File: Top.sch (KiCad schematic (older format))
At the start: 0 parts

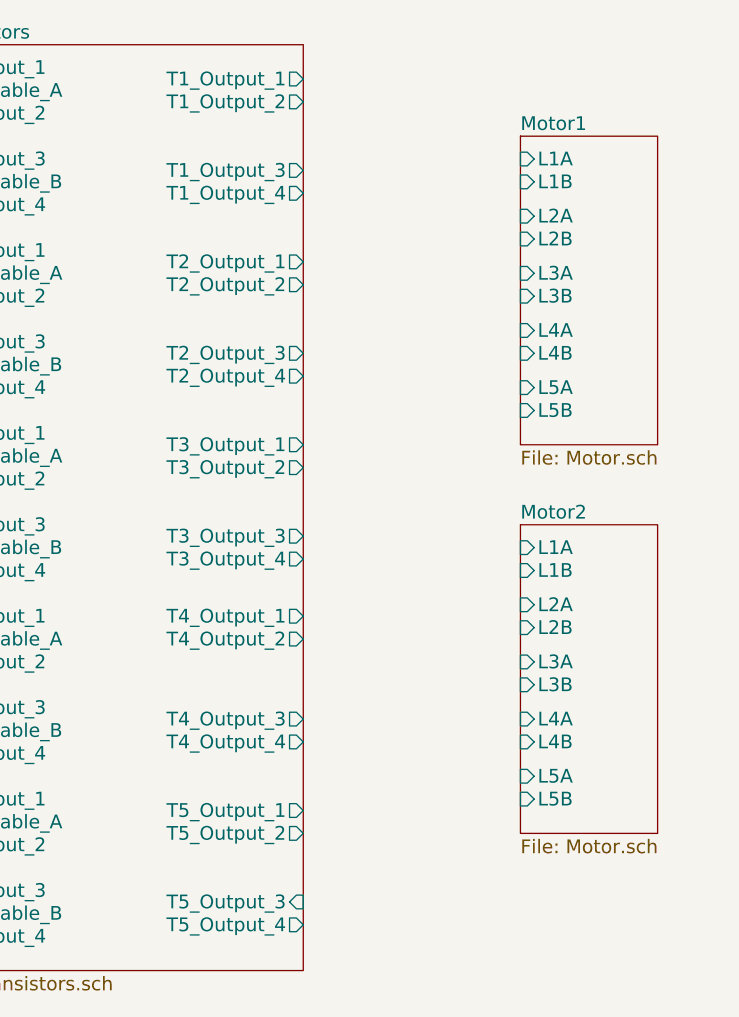
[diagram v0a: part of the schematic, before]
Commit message: Connected hierarchical labels in Top.sch Beautified label order in Transistors.sch
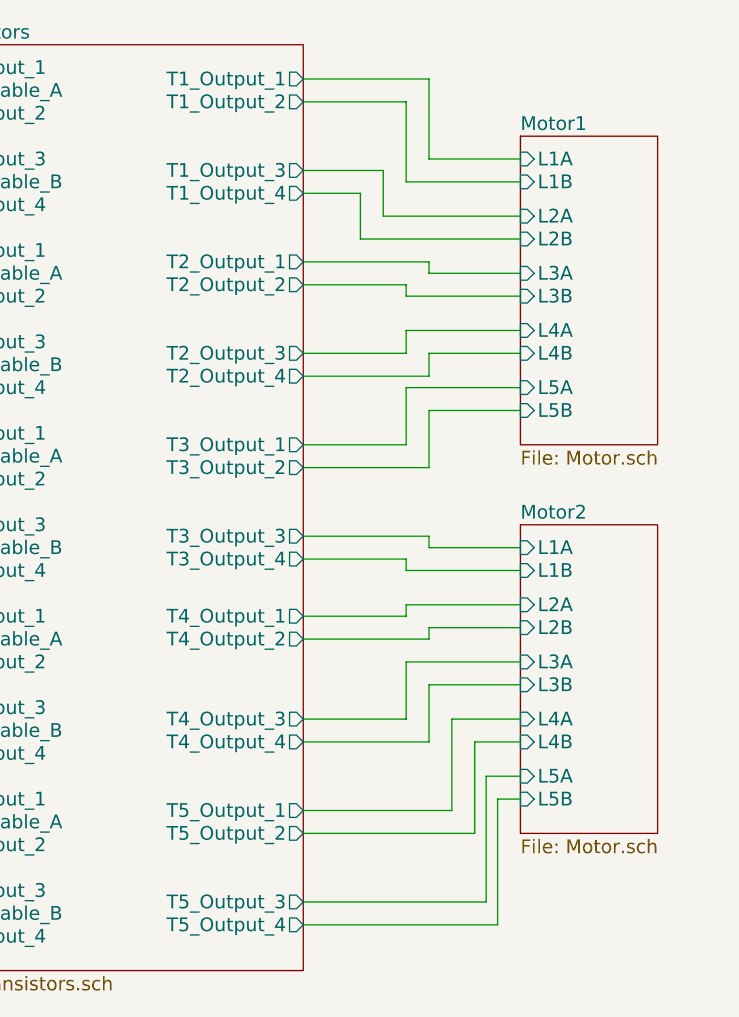
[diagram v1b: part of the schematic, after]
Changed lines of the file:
@@
 F33 "T4_Output_3" O R 6500 4900 60
 F34 "T4_Output_4" O R 6500 5000 60
-F35 "T5_Output_3" I R 6500 5700 60
-F36 "T4_Input_1" I L 4850 4450 60
-F37 "T4_Enable_A" I L 4850 4550 60
-F38 "T4_Input_2" I L 4850 4650 60
-F39 "T4_Input_3" I L 4850 4850 60
-F40 "T4_Enable_B" I L 4850 4950 60
-F41 "T4_Input_4" I L 4850 5050 60
-F42 "T5_Input_1" I L 4850 5250 60
-F43 "T5_Enable_A" I L 4850 5350 60
-F44 "T5_Input_2" I L 4850 5450 60
-F45 "T5_Input_3" I L 4850 5650 60
-F46 "T5_Enable_B" I L 4850 5750 60
-F47 "T5_Input_4" I L 4850 5850 60
-F48 "T1_Input_1" I L 4850 2050 60
-F49 "T5_Output_1" O R 6500 5300 60
-F50 "T5_Output_2" O R 6500 5400 60
-F51 "T5_Output_4" O R 6500 5800 60
+F35 "T4_Input_1" I L 4850 4450 60
+F36 "T4_Enable_A" I L 4850 4550 60
+F37 "T4_Input_2" I L 4850 4650 60
+F38 "T4_Input_3" I L 4850 4850 60
+F39 "T4_Enable_B" I L 4850 4950 60
+F40 "T4_Input_4" I L 4850 5050 60
+F41 "T5_Input_1" I L 4850 5250 60
+F42 "T5_Enable_A" I L 4850 5350 60
+F43 "T5_Input_2" I L 4850 5450 60
+F44 "T5_Input_3" I L 4850 5650 60
+F45 "T5_Enable_B" I L 4850 5750 60
+F46 "T5_Input_4" I L 4850 5850 60
+F47 "T1_Input_1" I L 4850 2050 60
+F48 "T5_Output_1" O R 6500 5300 60
+F49 "T5_Output_2" O R 6500 5400 60
+F50 "T5_Output_4" O R 6500 5800 60
+F51 "T5_Output_3" O R 6500 5700 60
 $EndSheet
+Wire Wire Line
+	6500 2100 7050 2100
+Wire Wire Line
+	7050 2100 7050 2450
+Wire Wire Line
+	7050 2450 7450 2450
+Wire Wire Line
+	7450 2550 6950 2550
+Wire Wire Line
+	6950 2550 6950 2200
+Wire Wire Line
+	6950 2200 6500 2200
+Wire Wire Line
+	6500 2500 6850 2500
+Wire Wire Line
+	6850 2500 6850 2700
+Wire Wire Line
+	6850 2700 7450 2700
+Wire Wire Line
+	7450 2800 6750 2800
+Wire Wire Line
+	6750 2800 6750 2600
+Wire Wire Line
+	6750 2600 6500 2600
+Wire Wire Line
+	6500 2900 7050 2900
+Wire Wire Line
+	7050 2900 7050 2950
+Wire Wire Line
+	7050 2950 7450 2950
+Wire Wire Line
+	7450 3050 6950 3050
+Wire Wire Line
+	6950 3050 6950 3000
+Wire Wire Line
+	6950 3000 6500 3000
+Wire Wire Line
+	6500 3300 6950 3300
+Wire Wire Line
+	6950 3300 6950 3200
+Wire Wire Line
+	6950 3200 7450 3200
+Wire Wire Line
+	7450 3300 7050 3300
+Wire Wire Line
+	7050 3300 7050 3400
+Wire Wire Line
+	7050 3400 6500 3400
+Wire Wire Line
+	6500 3700 6950 3700
+Wire Wire Line
+	6950 3700 6950 3450
+Wire Wire Line
+	6950 3450 7450 3450
+Wire Wire Line
+	7450 3550 7050 3550
+Wire Wire Line
+	7050 3550 7050 3800
+Wire Wire Line
+	7050 3800 6500 3800
+Wire Wire Line
+	6500 4100 7050 4100
+Wire Wire Line
+	7050 4100 7050 4150
+Wire Wire Line
+	7050 4150 7450 4150
+Wire Wire Line
+	7450 4250 6950 4250
+Wire Wire Line
+	6950 4250 6950 4200
+Wire Wire Line
+	6950 4200 6500 4200
+Wire Wire Line
+	6500 4450 6950 4450
+Wire Wire Line
+	6950 4450 6950 4400
+Wire Wire Line
+	6950 4400 7450 4400
+Wire Wire Line
+	7450 4500 7050 4500
+Wire Wire Line
+	7050 4500 7050 4550
+Wire Wire Line
+	7050 4550 6500 4550
+Wire Wire Line
+	6500 4900 6950 4900
+Wire Wire Line
+	6950 4900 6950 4650
+Wire Wire Line
+	6950 4650 7450 4650
+Wire Wire Line
+	7450 4750 7050 4750
+Wire Wire Line
+	7050 4750 7050 5000
+Wire Wire Line
+	7050 5000 6500 5000
+Wire Wire Line
+	6500 5300 7150 5300
+Wire Wire Line
+	7150 5300 7150 4900
+Wire Wire Line
+	7150 4900 7450 4900
+Wire Wire Line
+	7450 5000 7250 5000
+Wire Wire Line
+	7250 5000 7250 5400
+Wire Wire Line
+	7250 5400 6500 5400
+Wire Wire Line
+	6500 5700 7300 5700
+Wire Wire Line
+	7300 5700 7300 5150
+Wire Wire Line
+	7300 5150 7450 5150
+Wire Wire Line
+	7450 5250 7350 5250
+Wire Wire Line
+	7350 5250 7350 5800
+Wire Wire Line
+	7350 5800 6500 5800
 $EndSCHEMATC

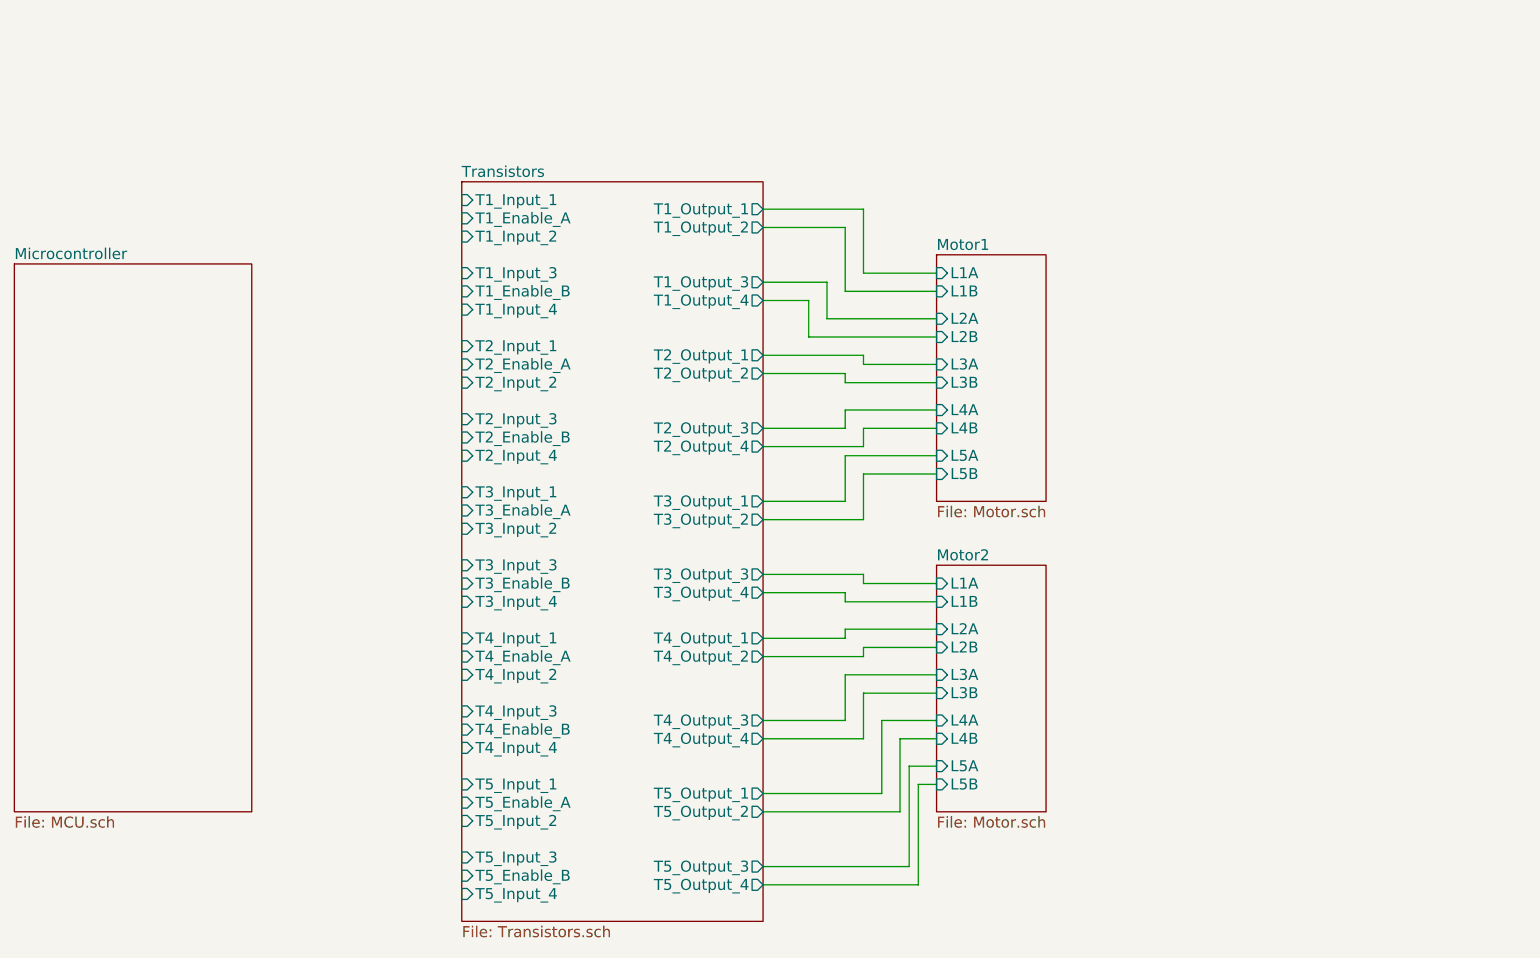
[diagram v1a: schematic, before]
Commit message: Added and connected sixth L298N symbol
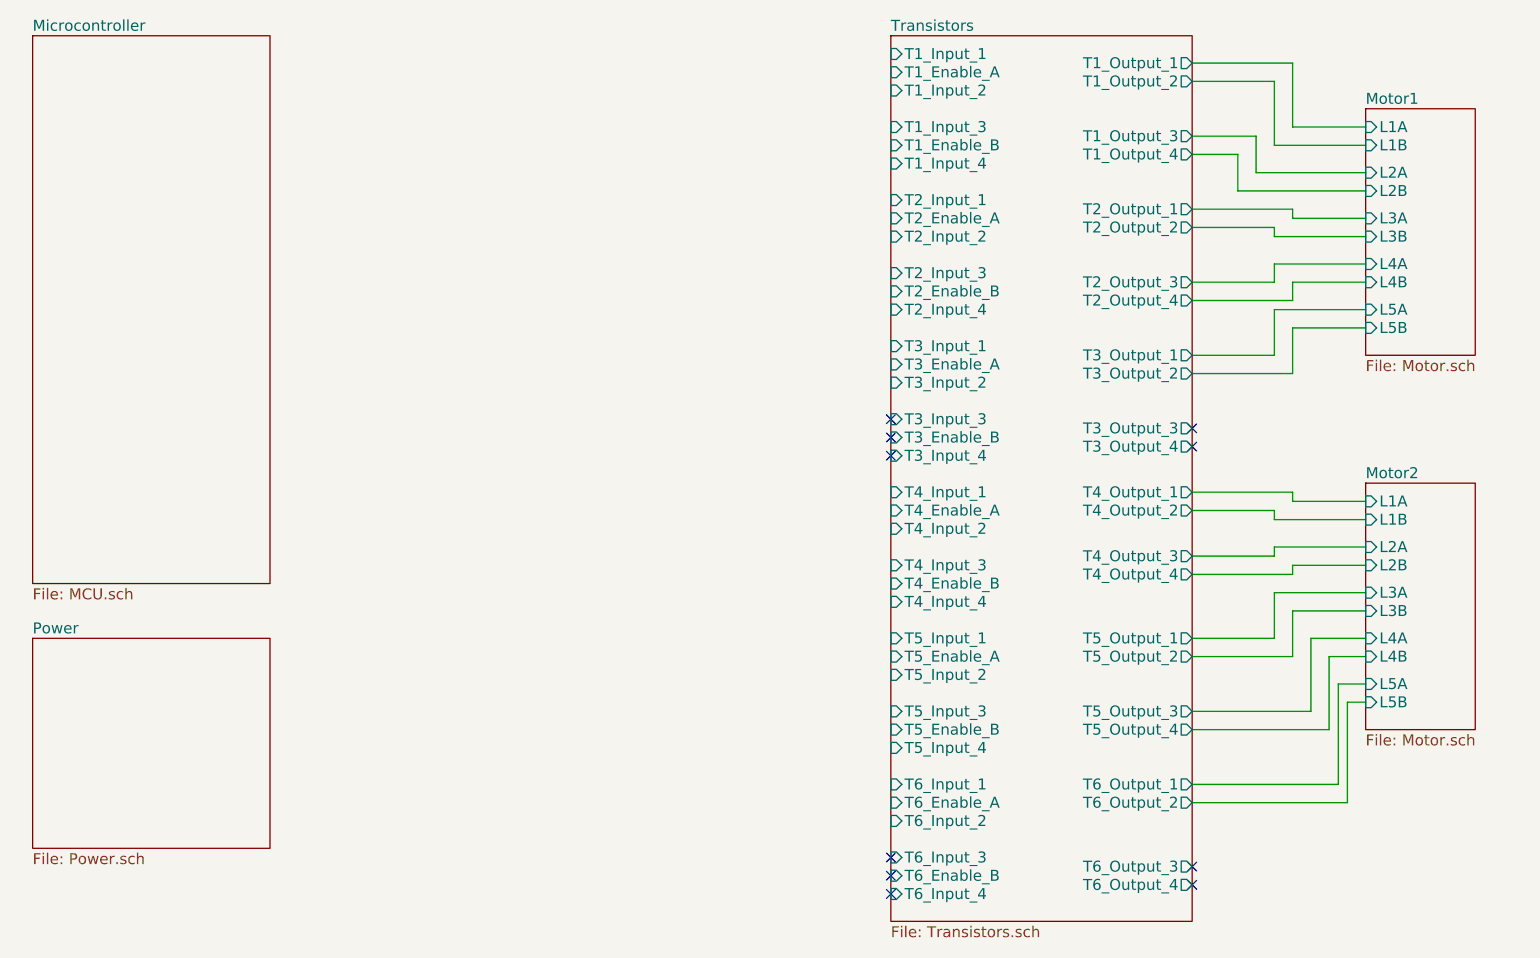
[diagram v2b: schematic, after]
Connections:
- no-connect marks 0 -> 10
